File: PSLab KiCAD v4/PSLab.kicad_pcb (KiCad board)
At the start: 4 copper layers, 99 x 53.3 mm, 150 parts, among them CON1 USB-MINI-B, J1 Programmer, J10 GND, J11 Vbus, J13 D+, J14 D-, J15 PCs, J16 I2C-2, J2 DoublePins, J3 LA, J4 Outputs, J6 I2C-1, J8 Conn_01x07, J9 PVs, P7 NRF, Q1 MMBT3906, Q2 MMBT3904, Q3 MMBT3906, U1 MCP2200, U10 TL082, U11 6S21, U12 6S21, U13 TL082, U15 ESP8266, U16 TL082, U2 74HC126, U3 PIC24EP256GP204, U4 TC1240A, U5 7660, U6 LM1117-3.3, U7 LM324, U8 TL082, U9 MCP4728, X1 12MHz, Y1 12MHz

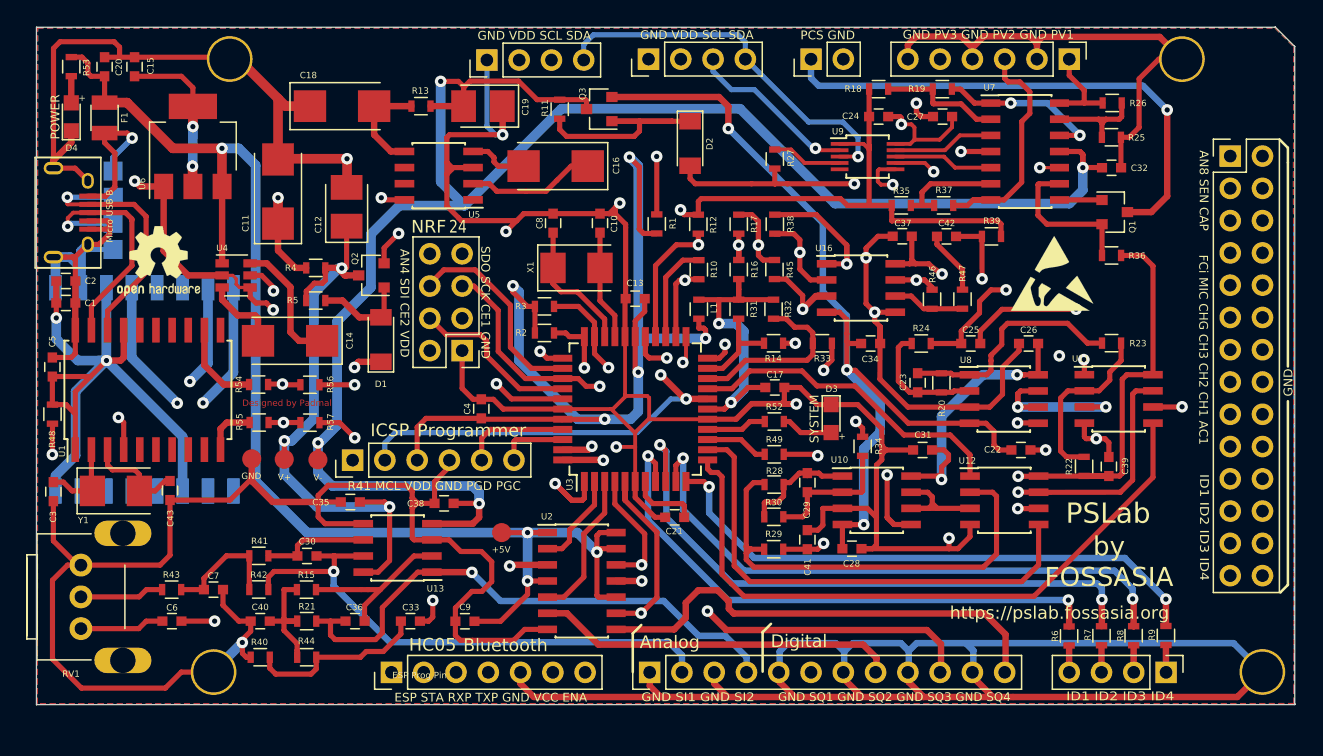
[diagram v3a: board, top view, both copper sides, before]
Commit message: Added FOSSASIA Logo and updated BoM
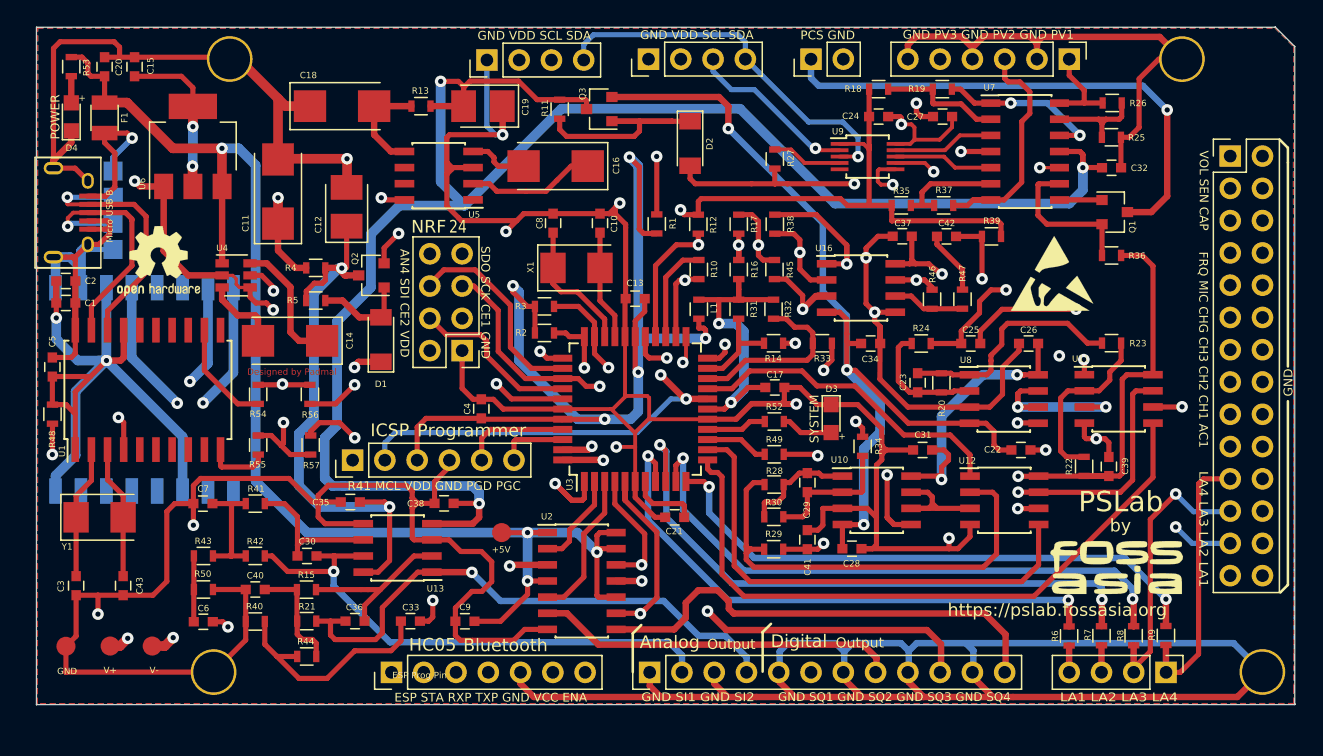
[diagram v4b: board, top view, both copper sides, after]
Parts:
- removed RV1: POT, Potentiometers:Potentiometer_Alps_RK09K_Vertical
- added G***: LOGO, Custom_Components:A25015, F.Cu at (175.9, 102.7)
- added G***: LOGO, Custom_Components:A25015, B.Cu at (117.3, 87.3)
- added G***: LOGO, Custom_Components:QR, B.Cu at (140.2, 86.6)
- added R50: 200K, Resistors_SMD:R_0603, F.Cu at (104.1, 104.5)
- C10, C8: value 33pF -> 33p
- R48: value 5k1 -> 5K1
- moved TP4 20.8 mm to (93.3, 109.0)
- moved TP2 20.1 mm to (96.7, 109.0)
- moved TP1 19.6 mm to (100.0, 109.0)
- moved C43 8.35 mm to (97.8, 104.2)
- moved C3 7.61 mm to (94.1, 104.2)
- moved C7 6.82 mm to (104.0, 97.8), turned to 180 degrees
- moved R41 4.12 mm to (108.2, 97.8)
- moved R43 3.64 mm to (104.1, 101.9)
- moved R40 2.84 mm to (108.2, 107.0)
- moved R42 2.65 mm to (108.2, 101.9)
- moved C40 2.52 mm to (108.2, 104.5)
- moved C6 2.47 mm to (104.1, 107.1)
- moved Y1 2.44 mm to (95.9, 98.8)
- moved R55 1.77 mm to (108.4, 93.2), turned to 270 degrees
- moved R57 1.76 mm to (112.5, 93.2), turned to 270 degrees
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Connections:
- J2 pad 21: IDA -> IDD
- J2 pad 23: IDB -> IDC
- J2 pad 25: IDC -> IDB
- J2 pad 27: IDD -> IDA
- J8 pad 2: (no net) -> Net-(J8-Pad2)
- J8 pad 7: (no net) -> Net-(J8-Pad7)
- R43 pad 1: Net-(R43-Pad1) -> Net-(C6-Pad2)
- U1 pad 11: (no net) -> Net-(U1-Pad11)
- U1 pad 13: (no net) -> Net-(U1-Pad13)
- U1 pad 14: (no net) -> Net-(U1-Pad14)
- U1 pad 15: (no net) -> Net-(U1-Pad15)
- U1 pad 16: (no net) -> Net-(U1-Pad16)
- U1 pad 5: (no net) -> Net-(U1-Pad5)
- U1 pad 6: (no net) -> Net-(U1-Pad6)
- U1 pad 7: (no net) -> Net-(U1-Pad7)
- U1 pad 8: (no net) -> Net-(U1-Pad8)
- U1 pad 9: (no net) -> Net-(U1-Pad9)
- U15 pad 1: (no net) -> Net-(U15-Pad1)
- U15 pad 13: (no net) -> Net-(U15-Pad13)
- U15 pad 14: (no net) -> Net-(U15-Pad14)
- U15 pad 2: (no net) -> Net-(U15-Pad2)
- U15 pad 4: (no net) -> Net-(U15-Pad4)
- U15 pad 5: (no net) -> Net-(U15-Pad5)
- U15 pad 6: (no net) -> Net-(U15-Pad6)
- U15 pad 7: (no net) -> Net-(U15-Pad7)
- U5 pad 1: (no net) -> Net-(U5-Pad1)
- U5 pad 6: (no net) -> Net-(U5-Pad6)
- U5 pad 7: (no net) -> Net-(U5-Pad7)
- U9 pad 5: (no net) -> Net-(U9-Pad5)
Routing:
- net V-: track 144.8 -> 173.8 mm
- net V+: track 135.7 -> 160.5 mm
- net IDD: track 12.9 -> 21.4 mm
- net GND: track 803.0 -> 795.4 mm, vias 18 -> 19
- net Net-(R43-Pad1): track 6.63 -> 0.00 mm
- net IDB: track 21.8 -> 26.7 mm, vias 0 -> 1
- net IDC: track 17.5 -> 22.5 mm, vias 0 -> 1
- net /TxD: track 67.2 -> 71.3 mm
- net OS1: track 6.64 -> 10.5 mm
- net Net-(C33-Pad2): track 14.2 -> 18.0 mm
- net Net-(C30-Pad2): track 8.48 -> 11.5 mm
- net OS2: track 8.05 -> 10.5 mm
- net IDA: track 26.5 -> 24.2 mm
- net /MRxD: track 6.90 -> 8.50 mm
- net /RxD: track 69.3 -> 70.9 mm
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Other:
- board text added: "Bluetooth EN"
- board text added: "Bluetooth Rx"
- board text added: "Bluetooth STATE"
- board text added: "Bluetooth Tx"
- board text added: "Capacitance"
- board text added: "Channel 3 Gain Set"
- board text added: "Current Source (0-3.3)mA"
- board text added: "ESP Program"
- board text added: "FRQ MIC CHG CH3 CH2 CH1 AC1"
- board text added: "Frequency Count"
- board text added: "Ground - 0V"
- board text added: "I2C"
- board text added: "LA - 1"
- board text added: "LA - 2"
- board text added: "LA - 3"
- board text added: "LA - 4"
- board text added: "LA1 LA2 LA3 LA4"
- board text added: "LA4 LA3 LA2 LA1"
- board text added: "Logic Analyzer - 1"
- board text added: "Logic Analyzer - 2"
- board text added: "Logic Analyzer - 3"
- board text added: "Logic Analyzer - 4"
- board text added: "Microphone Input"
- board text added: "Oscilloscope Alternative Wave Input"
- board text added: "Oscilloscope Channel 1 Input (-/+16)V"
- board text added: "Oscilloscope Channel 2 Input (-/+16)V"
- board text added: "Oscilloscope Channel 3 Input (-/+16)V"
- board text added: "Output"
- board text added: "Pocket Science Lab"
- board text added: "Power Outputs"
- board text added: "Resistance"
- board text added: "SCL for I2C"
- board text added: "SDA for I2C"
- board text added: "Sine Wave - 1"
- board text added: "Sine Wave - 2"
- board text added: "Square Wave - 1"
- board text added: "Square Wave - 2"
- board text added: "Square Wave - 3"
- board text added: "Square Wave - 4"
- board text added: "VCC (+5V)"
- board text added: "VDD - 3.3V"
- board text added: "VOL SEN CAP"
- board text added: "Voltage Source 1 (-/+5)V"
- board text added: "Voltage Source 2 (-/+3.3)V"
- board text added: "Voltage Source 3 (0-3.3)V"
- board text added: "Voltmeter"
- board text added: "Wave Generator"
- board text added: "by"
- board text removed: "5th Rev @ 21 Apr '18"
- board text removed: "AN8 SEN CAP"
- board text removed: "FCi MIC CHG CH3 CH2 CH1 AC1"
- board text removed: "ID1 ID2 ID3 ID4"
- board text removed: "by FOSSASIA"

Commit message: NRF replaced with Bluetooth
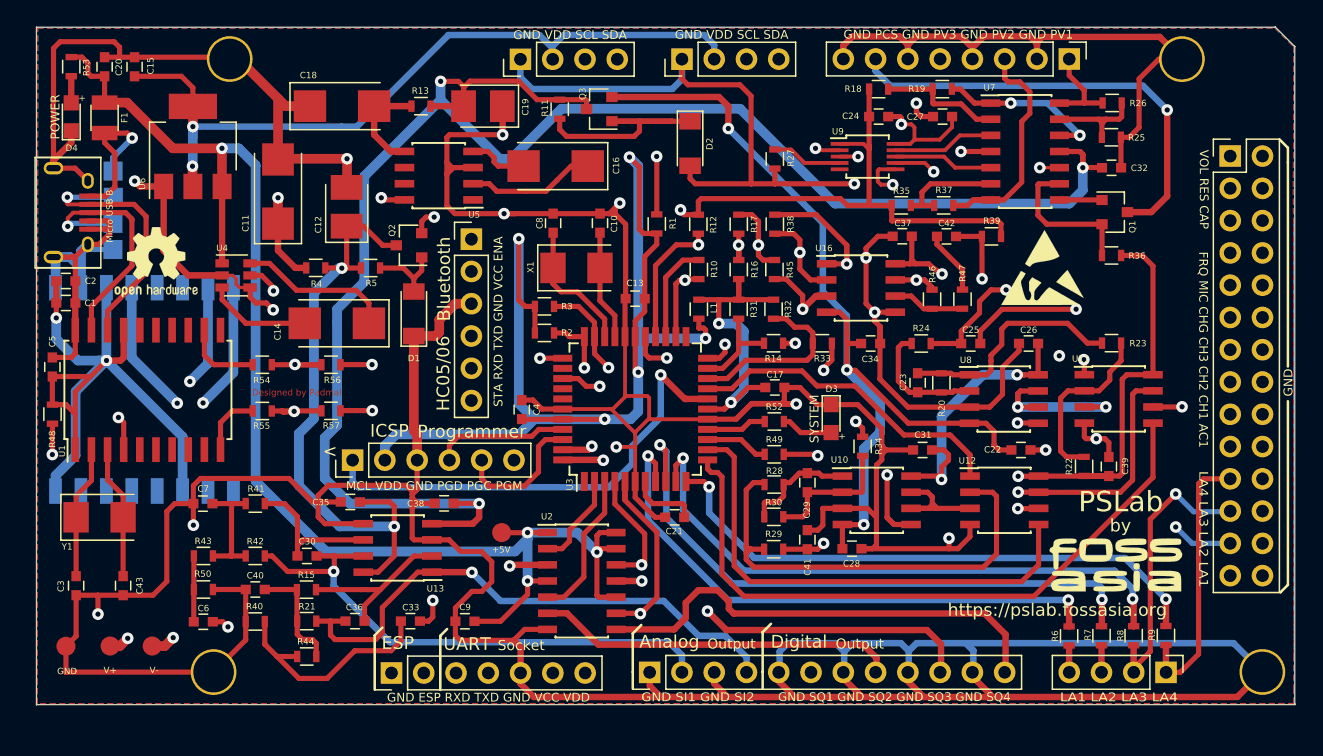
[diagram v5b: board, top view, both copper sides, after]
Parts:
- removed the G*** at (175.9, 102.7)
- removed the G*** at (117.3, 87.3)
- removed J15: PCs, Pin_Headers:Pin_Header_Straight_1x02_Pitch2.54mm
- removed J9: PVs, Pin_Headers:Pin_Header_Straight_1x06_Pitch2.54mm
- removed P7: NRF, Pin_Headers:Pin_Header_Straight_2x04_Pitch2.54mm
- added G***: LOGO, Custom_Components:FOSSASIA_Logo, F.Cu at (175.8, 102.5)
- added G***: LOGO, Custom_Components:FOSSASIA_Logo, B.Cu at (117.3, 87.2)
- added J5: Bluetooth, Pin_Headers:Pin_Header_Straight_1x06_Pitch2.54mm, F.Cu at (125.2, 77.0)
- added J7: UART/ESP, Pin_Headers:Pin_Header_Straight_1x07_Pitch2.54mm, F.Cu at (118.9, 111.1)
- J8: value Conn_01x07 -> Power Pins; footprint Pin_Headers:Pin_Header_Straight_1x07_Pitch2.54mm -> Pin_Headers:Pin_Header_Straight_1x08_Pitch2.54mm
- moved J8 71.9 mm to (172.2, 62.8), turned to 270 degrees
- moved R5 5.01 mm to (117.2, 79.2)
- moved C14 3.93 mm to (114.6, 83.6)
- moved Q2 3.79 mm to (120.3, 77.4)
- moved D1 3.29 mm to (120.6, 82.8)
- moved C4 3.18 mm to (129.1, 90.4)
- moved R57 3.13 mm to (114.1, 90.5), turned to 180 degrees
- moved R56 2.86 mm to (114.1, 86.8), turned to 180 degrees
- moved R55 2.70 mm to (108.7, 90.5), turned to 180 degrees
- moved J6 2.64 mm to (129.0, 62.8)
- moved J16 2.63 mm to (141.7, 62.8)
- moved R54 2.35 mm to (108.7, 86.8), turned to 180 degrees
- moved REF*** 0.89 mm to (170.1, 79.2)
- moved G*** 0.42 mm to (140.2, 87.0)
- moved REF*** 0.21 mm to (100.4, 78.8)
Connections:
- J1 pad 1: RP41 -> MCLR
- J1 pad 2: MCLR -> Vdd
- J1 pad 3: Vdd -> GND
- J1 pad 4: GND -> PGD2
- J1 pad 5: PGD2 -> PGC2
- J1 pad 6: PGC2 -> Net-(J1-Pad6)
- J8 pad 1: /ESPROG -> PVS1
- J8 pad 2: Net-(J8-Pad2) -> GND
- J8 pad 3: /RxD -> PVS2
- J8 pad 4: /TxD -> GND
- J8 pad 5: GND -> PVS3
- J8 pad 6: +5V -> GND
- J8 pad 7: Net-(J8-Pad7) -> PCS
- R54 pad 1: /RxD -> RxD
- R55 pad 1: /TxD -> TxD
- R56 pad 2: /RxD -> RxD
- R57 pad 2: /TxD -> TxD
- U3 pad 1: RP41 -> Net-(U3-Pad1)
- U3 pad 23: AN4 -> Net-(U3-Pad23)
- U3 pad 35: SDI -> Net-(U3-Pad35)
- U3 pad 37: CS.E2 -> Net-(U3-Pad37)
- U3 pad 38: CS.E1 -> Net-(U3-Pad38)
- U3 pad 43: /RxD -> RxD
- U3 pad 44: /TxD -> TxD
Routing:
- net RxD: track 0.00 -> 75.8 mm, vias 0 -> 2
- net TxD: track 0.00 -> 75.2 mm, vias 0 -> 2
- net /TxD: track 71.3 -> 0.00 mm, vias 2 -> 0
- net /RxD: track 70.9 -> 0.00 mm, vias 2 -> 0
- net Vdd: track 228.9 -> 299.4 mm
- net AN4: track 32.5 -> 0.00 mm, vias 1 -> 0
- net +5V: track 115.8 -> 147.1 mm
- net RP41: track 24.6 -> 0.00 mm, vias 1 -> 0
- net GND: track 795.4 -> 816.5 mm, vias 19 -> 18
- net AN8: track 121.6 -> 103.6 mm
- net SDI: track 16.3 -> 0.00 mm
- net CS.E2: track 13.4 -> 0.00 mm
- net V+: track 160.5 -> 147.1 mm
- net SCK: track 70.3 -> 57.4 mm
- net CS.E1: track 12.8 -> 0.00 mm, vias 1 -> 0
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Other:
- board text added: "<"
- board text added: "ESP"
- board text added: "GND ESP RXD TXD GND VCC VDD"
- board text added: "GND PCS GND PV3 GND PV2 GND PV1"
- board text added: "HC05/06"
- board text added: "MCL VDD GND PGD PGC PGM"
- board text added: "STA RXD TXD GND VCC ENA"
- board text added: "Socket"
- board text added: "UART"
- board text added: "UART Rx"
- board text added: "UART Tx"
- board text added: "VCC"
- board text added: "VDD (+3.3V)"
- board text added: "VOL RES CAP"
- board text removed: "24"
- board text removed: "AN4 SDI CE2 VDD"
- board text removed: "Bluetooth EN"
- board text removed: "Bluetooth Rx"
- board text removed: "Bluetooth STATE"
- board text removed: "Bluetooth Tx"
- board text removed: "ESP Prog Pin"
- board text removed: "ESP STA RXP TXP GND VCC ENA"
- board text removed: "GND PV3 GND PV2 GND PV1"
- board text removed: "HC05"
- board text removed: "NRF"
- board text removed: "PCS GND"
- board text removed: "R41 MCL VDD GND PGD PGC"
- board text removed: "SDO SCK CE1 GND"
- board text removed: "VOL SEN CAP"
- board text removed: "Vbus"

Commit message: Modified silk screen texts
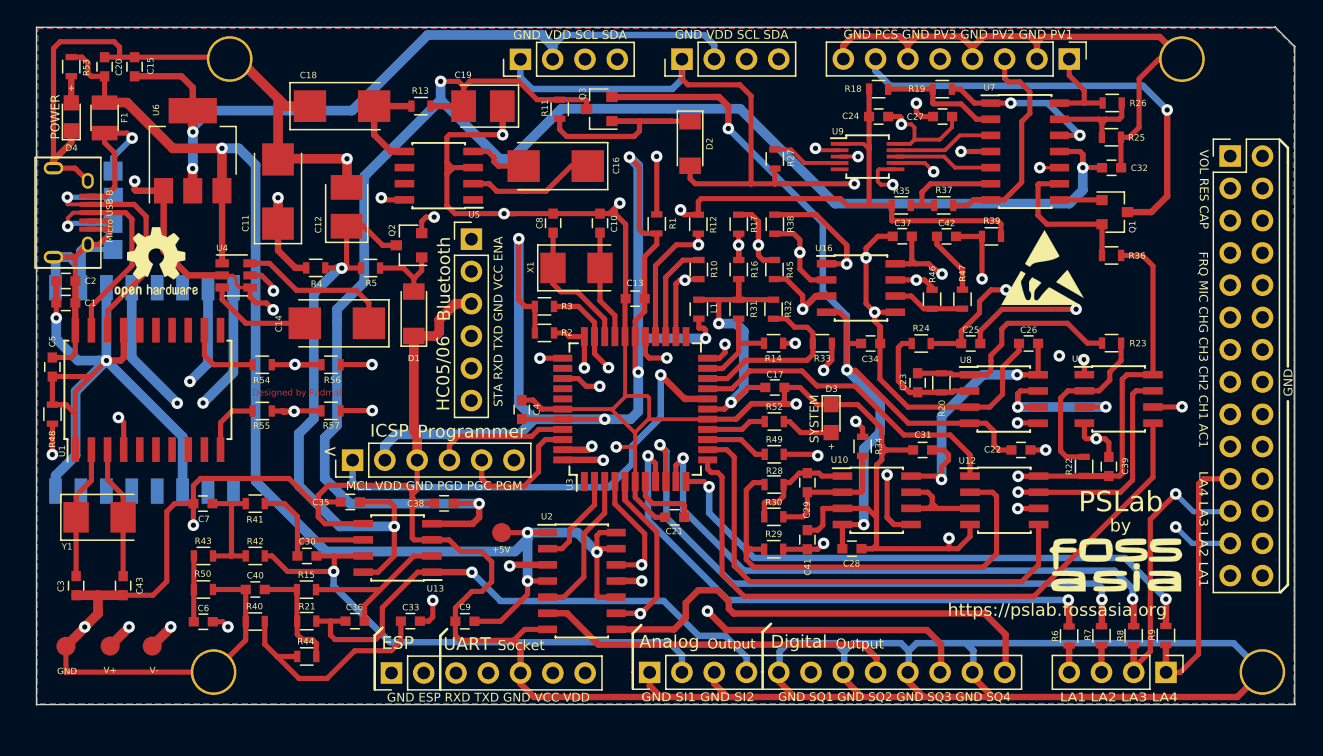
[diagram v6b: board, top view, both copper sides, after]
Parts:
- moved G*** 2.26 mm to (142.4, 86.6)
- moved U6 0.34 mm to (103.2, 70.0)
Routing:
- net GND: track 816.5 -> 820.0 mm
- net Vdd: track 299.4 -> 300.1 mm
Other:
- board text added: "AC Waves (±16)V"
- board text added: "CH1 (±16)V"
- board text added: "CH2 (±16)V"
- board text added: "CH3 (±16)V"
- board text added: "CH3 Gain Set"
- board text added: "Current (0-3.3)mA"
- board text added: "ENA"
- board text added: "Frequency"
- board text added: "Ground"
- board text added: "LA 1"
- board text added: "LA 2"
- board text added: "LA 3"
- board text added: "LA 4"
- board text added: "Logic Analyzer 1"
- board text added: "Logic Analyzer 2"
- board text added: "Logic Analyzer 3"
- board text added: "Logic Analyzer 4"
- board text added: "MCLR"
- board text added: "Microphone"
- board text added: "PGC"
- board text added: "PGD"
- board text added: "PGM"
- board text added: "RXD"
- board text added: "STA"
- board text added: "Sine Wave 1"
- board text added: "Sine Wave 2"
- board text added: "Square Wave 1"
- board text added: "Square Wave 2"
- board text added: "Square Wave 3"
- board text added: "Square Wave 4"
- board text added: "TXD"
- board text added: "VDD"
- board text added: "Voltage 1 (±5)V"
- board text added: "Voltage 2 (±3.3)V"
- board text added: "Voltage 3 (0-3.3)V"
- board text removed: "Channel 3 Gain Set"
- board text removed: "Current Source (0-3.3)mA"
- board text removed: "ESP Program"
- board text removed: "Frequency Count"
- board text removed: "Ground - 0V"
- board text removed: "LA - 1"
- board text removed: "LA - 2"
- board text removed: "LA - 3"
- board text removed: "LA - 4"
- board text removed: "Logic Analyzer - 1"
- board text removed: "Logic Analyzer - 2"
- board text removed: "Logic Analyzer - 3"
- board text removed: "Logic Analyzer - 4"
- board text removed: "Microphone Input"
- board text removed: "Oscilloscope Alternative Wave Input"
- board text removed: "Oscilloscope Channel 1 Input (-/+16)V"
- board text removed: "Oscilloscope Channel 2 Input (-/+16)V"
- board text removed: "Oscilloscope Channel 3 Input (-/+16)V"
- board text removed: "Sine Wave - 1"
- board text removed: "Sine Wave - 2"
- board text removed: "Square Wave - 1"
- board text removed: "Square Wave - 2"
- board text removed: "Square Wave - 3"
- board text removed: "Square Wave - 4"
- board text removed: "VDD - 3.3V"
- board text removed: "Voltage Source 1 (-/+5)V"
- board text removed: "Voltage Source 2 (-/+3.3)V"
- board text removed: "Voltage Source 3 (0-3.3)V"

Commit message: fix: updated pin layout diagram
added v4 pin layout

added missing GND pin

added pslabdesign.png

enhanced kicad fossasia logo
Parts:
- removed the G*** at (175.8, 102.5)
- removed the G*** at (117.3, 87.2)
- added G***: LOGO, Custom_Components:FOSSASIA_Logo, F.Cu at (176.1, 102.6)
- added G***: LOGO, Custom_Components:FOSSASIA_Logo, B.Cu at (117.2, 87.5)
